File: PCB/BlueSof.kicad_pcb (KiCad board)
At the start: 2 copper layers, 137.2 x 109.2 mm, 66 parts, among them SW1 SW_PUSH, SW10 SW_PUSH, SW11 SW_PUSH, SW12 SW_PUSH, SW13 SW_PUSH, SW14 SW_PUSH, SW15 SW_PUSH, SW16 SW_PUSH, SW17 SW_PUSH, SW18 SW_PUSH, SW19 SW_PUSH, SW2 SW_PUSH, SW20 SW_PUSH, SW21 SW_PUSH, SW22 SW_PUSH, SW23 SW_PUSH, SW24 SW_PUSH, SW25 Rotary_Encoder_Switch, SW26 SW_PUSH, SW27 SW_PUSH, SW28 SW_PUSH, SW29 SW_PUSH, SW3 SW_PUSH, SW30 SW_PUSH, SW4 SW_PUSH, SW5 SW_PUSH, SW6 SW_PUSH, SW7 SW_PUSH, SW8 SW_PUSH, SW9 SW_PUSH

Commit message: initial layout
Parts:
- removed TH1, TH3, TH4, TH5, TH6, TH7: HOLE, MountingHole:MountingHole_4mm
- added C1: 4.7uF, Capacitor_SMD:C_0603_1608Metric_Pad1.08x0.95mm_HandSolder, F.Cu at (103.5, 62.0)
- added C2: 4.7uF, Capacitor_SMD:C_0603_1608Metric_Pad1.08x0.95mm_HandSolder, F.Cu at (110.5, 56.9)
- added C3: 22pF, Capacitor_SMD:C_0603_1608Metric_Pad1.08x0.95mm_HandSolder, F.Cu at (110.5, 110.3)
- added C4: 22pF, Capacitor_SMD:C_0603_1608Metric_Pad1.08x0.95mm_HandSolder, F.Cu at (112.4, 114.9)
- added C5: 10uF, Capacitor_SMD:C_0603_1608Metric_Pad1.08x0.95mm_HandSolder, F.Cu at (106.0, 49.9)
- added D31: LED, LED_SMD:LED_0603_1608Metric_Pad1.05x0.95mm_HandSolder, F.Cu at (104.0, 49.9)
- added D32: LED, LED_SMD:LED_0603_1608Metric_Pad1.05x0.95mm_HandSolder, F.Cu at (91.0, 49.9)
- added D33: 1N5819, Diode_SMD:D_SOD-323_HandSoldering, F.Cu at (104.2, 57.9)
- added J1: USB_C_Receptacle_USB2.0, Connector_USB:USB_C_Receptacle_HRO_TYPE-C-31-M-12, F.Cu at (97.5, 50.4)
- added J2: Conn_01x01_Female, Connector_PinHeader_2.54mm:PinHeader_1x01_P2.54mm_Vertical, F.Cu at (95.0, 61.9)
- added J3: Conn_01x04_Female, Connector_PinHeader_2.54mm:PinHeader_1x04_P2.54mm_Vertical, F.Cu at (130.5, 82.7)
- added J4: Conn_01x01_Female, Connector_PinHeader_2.54mm:PinHeader_1x01_P2.54mm_Vertical, F.Cu at (106.2, 61.9)
- added Q2: A03407, Package_TO_SOT_SMD:SOT-23, F.Cu at (109.0, 53.4)
- added R1: 10k, Resistor_SMD:R_0603_1608Metric_Pad0.98x0.95mm_HandSolder, F.Cu at (104.0, 53.5)
- added R2: 10k, Resistor_SMD:R_0603_1608Metric_Pad0.98x0.95mm_HandSolder, F.Cu at (97.8, 62.1)
- added R4: 820k, Resistor_SMD:R_0603_1608Metric_Pad0.98x0.95mm_HandSolder, F.Cu at (107.5, 56.9)
- added R5: 2M, Resistor_SMD:R_0603_1608Metric_Pad0.98x0.95mm_HandSolder, F.Cu at (109.0, 56.9)
- added R6: 10k, Resistor_SMD:R_0603_1608Metric_Pad0.98x0.95mm_HandSolder, F.Cu at (91.0, 53.5)
- added R7: 5.1k, Resistor_SMD:R_0603_1608Metric_Pad0.98x0.95mm_HandSolder, F.Cu at (97.0, 57.9)
- added R8: 5.1k, Resistor_SMD:R_0603_1608Metric_Pad0.98x0.95mm_HandSolder, F.Cu at (93.4, 57.9)
- added R9: 100k, Resistor_SMD:R_0603_1608Metric_Pad0.98x0.95mm_HandSolder, F.Cu at (100.5, 57.9)
- added SW31: SW_Push, Button_Switch_SMD:SW_SPST_B3U-1000P, F.Cu at (92.5, 120.4)
- added U1: LN2054Y42AMR, Package_TO_SOT_SMD:SOT-23-5, F.Cu at (100.5, 62.1)
- added U2: E73-2G4M08S1C, BlueSof:E73-2G4M08S1C-52840, F.Cu at (108.0, 109.9)
- added U3: AP2112K-3.3, Package_TO_SOT_SMD:SOT-23-5, F.Cu at (109.0, 49.9)
- added Y1: 32.768kHz, Crystal:Crystal_SMD_MicroCrystal_CM9V-T1A-2Pin_1.6x1.0mm_HandSoldering, F.Cu at (109.5, 114.0)
- D1, D10, D11, D12, D13, D14, D15, D16, D17, D18, D19, D2, D20, D21, D22, D23, D24, D25, D26, D27, D28, D29, D3, D30, D4, D5, D6, D7, D8, D9: footprint SofleKeyboard-footprint:Diode_SOD123 -> BlueSof:Diode_SOD123
- SW1, SW10, SW11, SW12, SW13, SW14, SW15, SW16, SW17, SW18, SW19, SW2, SW20, SW21, SW22, SW23, SW24, SW27, SW28, SW29, SW3, SW30, SW4, SW5, SW6, SW7, SW8, SW9: footprint SofleKeyboard-footprint:KailhLowProfile -> BlueSof:KailhLowProfile
- SW26: footprint SofleKeyboard-footprint:KailhLowProfile -> BlueSof:KailhLowProfile_1.5U
- moved D25 21.1 mm to (111.0, 91.7), turned to 270 degrees
- moved SW25 9.51 mm to (93.0, 92.4)
- moved D26 5.41 mm to (112.5, 123.7)
- moved SW26 5.34 mm to (108.5, 126.2)
- moved SW27 1.00 mm to (130.0, 122.4), turned to 5 degrees
- moved SW30 0.80 mm to (185.0, 124.7)
- moved D27 0.26 mm to (129.7, 117.7), turned to 185 degrees
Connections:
- net SW25B renamed Net-(D25-Pad2)
- SW25 pad A: (no net) -> ENCA
- SW25 pad B: (no net) -> ENCB
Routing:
- removed copper zone on B.Cu, net GND
- removed copper zone on F.Cu, net GND
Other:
- board size 137.2 x 109.2 mm -> 132.5 x 106 mm
- board text added: "BlueSof v1 by ERL"
- board text removed: "Ellow Sofle Keyboard v1 by ERL"

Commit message: before 2nd side
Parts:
- moved + 15.0 mm to (110.0, 61.7)
- moved - 12.8 mm to (93.5, 61.7)
- moved Y1 0.27 mm to (109.5, 113.7)
- renumbered J2 to +, J4 to -
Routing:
- net VBUS: track 0.00 -> 91.9 mm
- net VDD_H: track 0.00 -> 72.0 mm
- net VBAT: track 0.00 -> 29.2 mm
- net Net-(C3-Pad2): track 0.00 -> 4.14 mm
- net Net-(C4-Pad2): track 0.00 -> 4.10 mm
- added copper zone on F.Cu, net (none)
- added copper zone on B.Cu, net GND

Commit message: EOD, layout on side 2 done, not routed
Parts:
- added C10: 10uF, Capacitor_SMD:C_0603_1608Metric_Pad1.08x0.95mm_HandSolder, B.Cu at (106.0, 49.9)
- added C6: 22pF, Capacitor_SMD:C_0603_1608Metric_Pad1.08x0.95mm_HandSolder, B.Cu at (111.1, 108.0)
- added C7: 22pF, Capacitor_SMD:C_0603_1608Metric_Pad1.08x0.95mm_HandSolder, B.Cu at (111.1, 104.4)
- added C8: 4.7uF, Capacitor_SMD:C_0603_1608Metric_Pad1.08x0.95mm_HandSolder, B.Cu at (103.5, 61.1)
- added C9: 4.7uF, Capacitor_SMD:C_0603_1608Metric_Pad1.08x0.95mm_HandSolder, B.Cu at (110.5, 56.9)
- added D34: LED, LED_SMD:LED_0603_1608Metric_Pad1.05x0.95mm_HandSolder, B.Cu at (91.7, 49.9)
- added D35: 1N5819, Diode_SMD:D_SOD-323_HandSoldering, B.Cu at (104.2, 57.1)
- added D36: LED, LED_SMD:LED_0603_1608Metric_Pad1.05x0.95mm_HandSolder, B.Cu at (90.2, 49.9)
- added J5: USB_C_Receptacle_USB2.0, Connector_USB:USB_C_Receptacle_HRO_TYPE-C-31-M-12, B.Cu at (97.8, 50.4)
- added Q1: A03407, Package_TO_SOT_SMD:SOT-23, B.Cu at (109.0, 53.4)
- added R10: 2M, Resistor_SMD:R_0603_1608Metric_Pad0.98x0.95mm_HandSolder, B.Cu at (109.0, 56.9)
- added R11: 10k, Resistor_SMD:R_0603_1608Metric_Pad0.98x0.95mm_HandSolder, B.Cu at (91.7, 53.5)
- added R12: 5.1k, Resistor_SMD:R_0603_1608Metric_Pad0.98x0.95mm_HandSolder, B.Cu at (97.0, 57.9)
- added R13: 5.1k, Resistor_SMD:R_0603_1608Metric_Pad0.98x0.95mm_HandSolder, B.Cu at (93.5, 57.9)
- added R14: 100k, Resistor_SMD:R_0603_1608Metric_Pad0.98x0.95mm_HandSolder, B.Cu at (100.5, 57.9)
- added R15: 10k, Resistor_SMD:R_0603_1608Metric_Pad0.98x0.95mm_HandSolder, B.Cu at (90.2, 53.5)
- added R16: 10k, Resistor_SMD:R_0603_1608Metric_Pad0.98x0.95mm_HandSolder, B.Cu at (97.8, 61.4)
- added R3: 820k, Resistor_SMD:R_0603_1608Metric_Pad0.98x0.95mm_HandSolder, B.Cu at (107.5, 56.9)
- added SW32: SW_Push, Button_Switch_SMD:SW_SPST_B3U-1000P, B.Cu at (92.5, 120.4)
- added U4: E73-2G4M08S1C, BlueSof:E73-2G4M08S1C-52840_NoInsidePads, B.Cu at (108.0, 109.9)
- added U5: LN2054Y42AMR, Package_TO_SOT_SMD:SOT-23-5, B.Cu at (100.5, 61.4)
- added U6: AP2112K-3.3, Package_TO_SOT_SMD:SOT-23-5, B.Cu at (109.0, 49.9)
- added Y2: 32.768kHz, Crystal:Crystal_SMD_MicroCrystal_CM9V-T1A-2Pin_1.6x1.0mm_HandSoldering, B.Cu at (109.4, 106.1)
- U2: footprint BlueSof:E73-2G4M08S1C-52840 -> BlueSof:E73-2G4M08S1C-52840_NoInsidePads
- moved D31 13.8 mm to (90.2, 49.9)
- moved R1 13.8 mm to (90.2, 53.5)
- moved C1 0.75 mm to (103.5, 61.3)
- moved R2 0.75 mm to (97.8, 61.4)
- moved U1 0.75 mm to (100.5, 61.4)
- moved D32 0.70 mm to (91.7, 49.9)
- moved R6 0.70 mm to (91.7, 53.5)
- moved J1 0.35 mm to (97.8, 50.4)
- renumbered + to J2, - to J4
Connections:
- J3 pad 3: (no net) -> SWD
- R2 pad 1: PROG -> Net-(R2-Pad1)
- U1 pad 5: PROG -> Net-(R2-Pad1)
- U2 pad 10: PROG -> ENCA
- U2 pad 15: ENCA -> P0.05_2
- U2 pad 17: ENCB -> row0
- U2 pad 26: (no net) -> RESET
- U2 pad 33: row0 -> row1
- U2 pad 35: row1 -> row2
- U2 pad 37: row2 -> SWD
- U2 pad 9: RESET -> ENCB
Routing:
- net VBUS: track 91.9 -> 0.00 mm
- net VDD_H: track 72.0 -> 0.00 mm
- net VBAT: track 29.2 -> 0.00 mm
- net Net-(C3-Pad2): track 4.14 -> 0.00 mm
- net Net-(C4-Pad2): track 4.10 -> 0.00 mm
- added copper zone on F.Cu, net Net-(U4-Pad42)
- removed copper zone on F.Cu, net (none)
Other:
- net class GND: clearance 0.2 -> 0.25; trace_width 0.5 -> 0.3
- net class VCC: clearance 0.2 -> 0.25; trace_width 0.5 -> 0.3

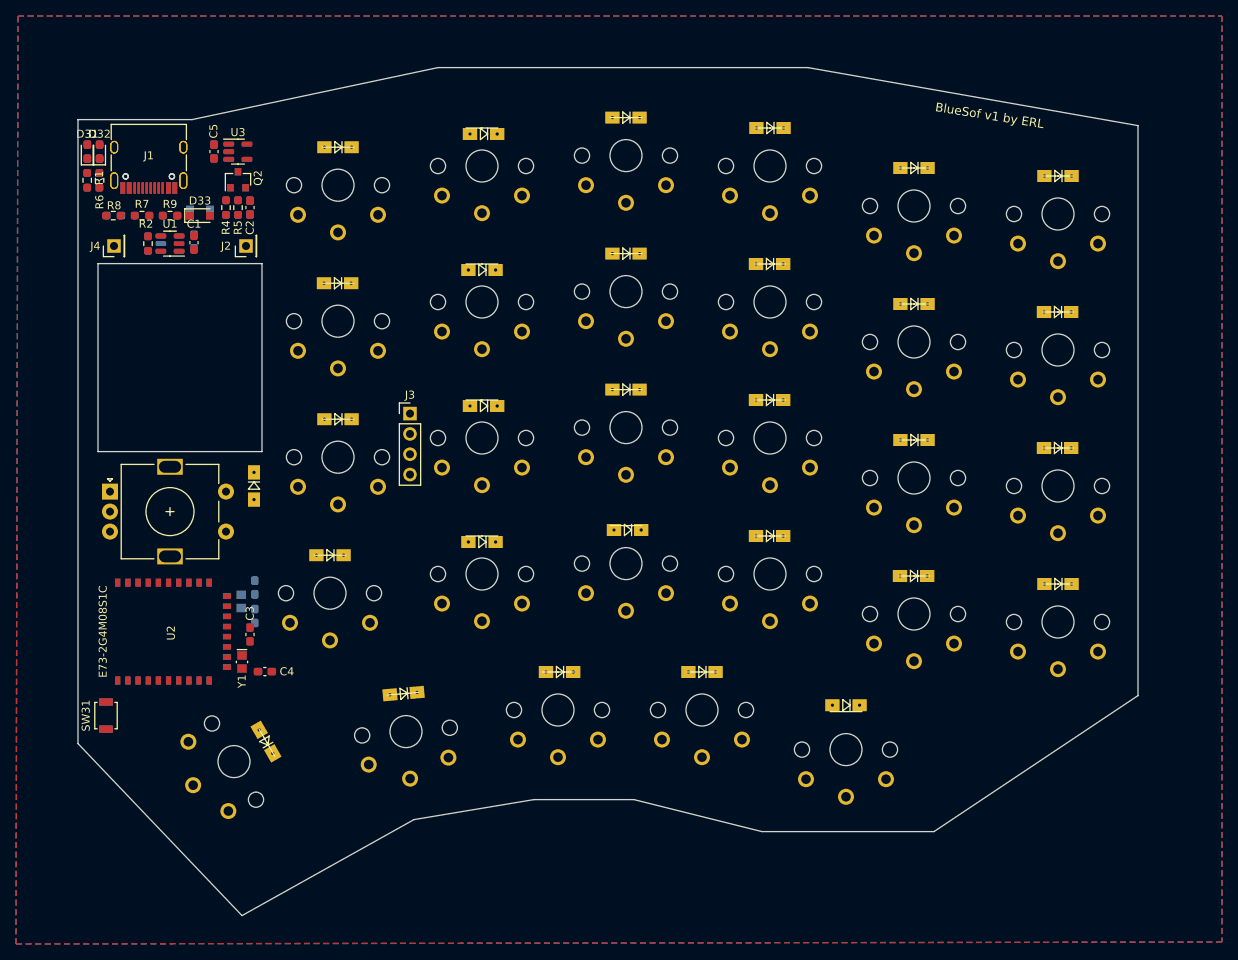
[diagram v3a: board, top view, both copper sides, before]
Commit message: autoroute done, still needs cleanup
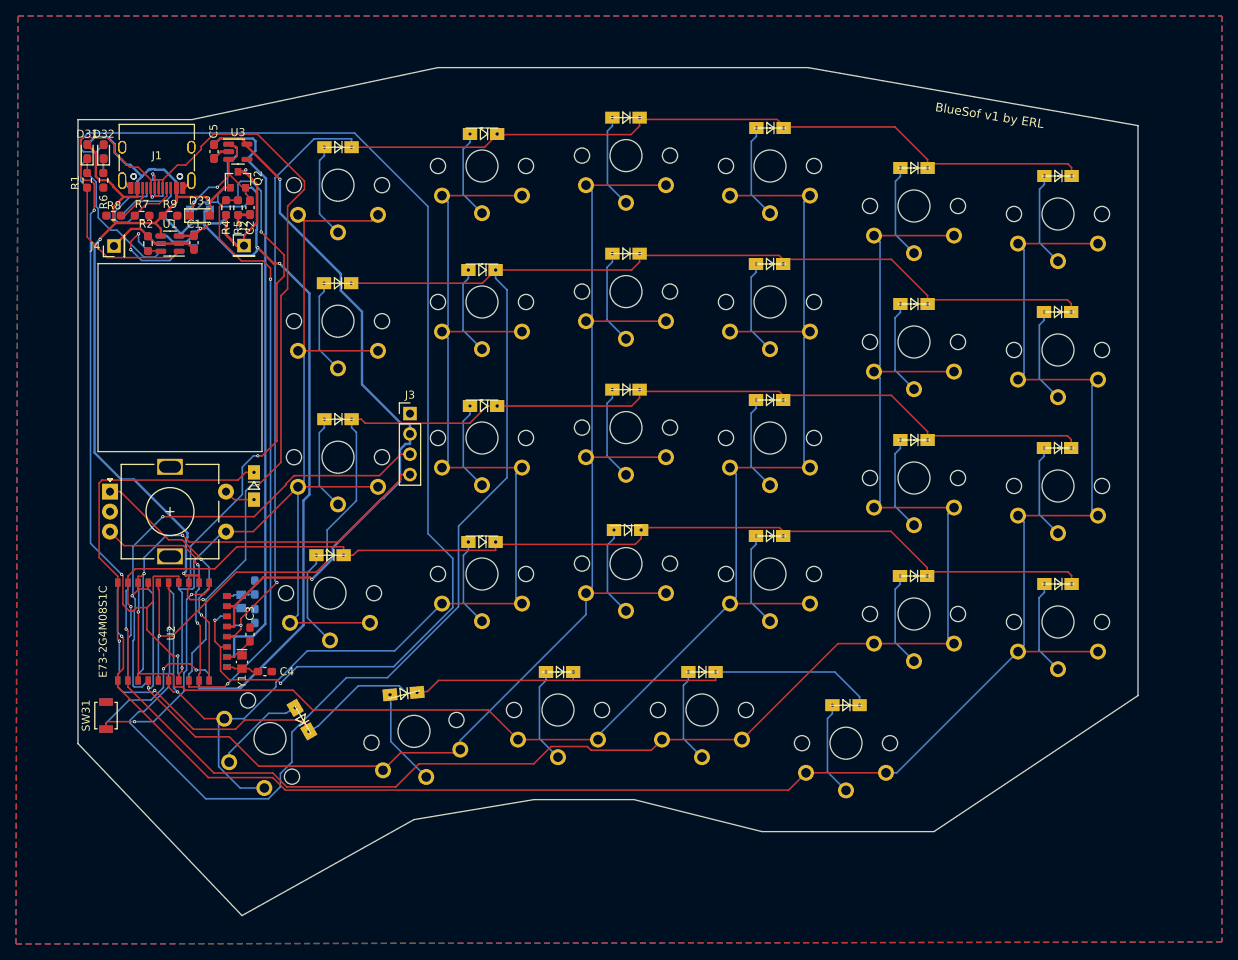
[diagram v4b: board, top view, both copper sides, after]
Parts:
- moved SW26 5.34 mm to (113.0, 123.3)
- moved D26 5.27 mm to (117.0, 120.9)
- moved SW27 1.00 mm to (131.0, 122.4), turned to 15 degrees
- moved J1 1.00 mm to (98.8, 50.4)
- moved J5 1.00 mm to (98.8, 50.4)
- moved SW30 0.80 mm to (185.0, 123.8)
- moved D32 0.50 mm to (92.2, 49.9)
- moved D34 0.50 mm to (92.2, 49.9)
- moved R11 0.50 mm to (92.2, 53.5)
- moved R6 0.50 mm to (92.2, 53.5)
- moved J2 0.25 mm to (109.8, 61.6), turned to 0 degrees
- turned R1 to 270 degrees
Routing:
- net col0: track 0.00 -> 231.5 mm, vias 0 -> 1
- net row1: track 0.00 -> 220.4 mm, vias 0 -> 1
- net col1: track 0.00 -> 212.3 mm, vias 0 -> 1
- net col2: track 0.00 -> 190.6 mm, vias 0 -> 1
- net col3: track 0.00 -> 178.2 mm, vias 0 -> 1
- net row0: track 0.00 -> 171.8 mm, vias 0 -> 2
- net col4: track 0.00 -> 163.0 mm, vias 0 -> 1
- net row2: track 0.00 -> 154.2 mm, vias 0 -> 2
- net row4: track 0.00 -> 150.6 mm, vias 0 -> 2
- net P0.05_2: track 0.00 -> 146.2 mm, vias 0 -> 2
- net row3: track 0.00 -> 141.8 mm, vias 0 -> 1
- net col5: track 0.00 -> 126.7 mm, vias 0 -> 1
- net VBUS2: track 0.00 -> 116.8 mm, vias 0 -> 2
- net DATA-: track 0.00 -> 103.6 mm, vias 0 -> 3
- net DATA+: track 0.00 -> 103.1 mm, vias 0 -> 4
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- added copper zone on F.Cu, net GND
- removed copper zone on F.Cu, net Net-(U4-Pad42)

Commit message: making progress on autoroute cleanup
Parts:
- added REF**: MountingHole_2.7mm_M2.5, MountingHole:MountingHole_2.7mm_M2.5, F.Cu at (96.3, 124.6)
- added REF**: MountingHole_2.7mm_M2.5, MountingHole:MountingHole_2.7mm_M2.5, F.Cu at (130.5, 111.1)
- added REF**: MountingHole_2.7mm_M2.5, MountingHole:MountingHole_2.7mm_M2.5, F.Cu at (202.5, 99.1)
- added REF**: MountingHole_2.7mm_M2.5, MountingHole:MountingHole_2.7mm_M2.5, F.Cu at (202.5, 66.1)
- added REF**: MountingHole_2.7mm_M2.5, MountingHole:MountingHole_2.7mm_M2.5, F.Cu at (130.5, 62.6)
- moved D26 4.54 mm to (113.0, 123.1)
- moved SW26 4.53 mm to (109.0, 125.4)
- moved C4 4.06 mm to (108.5, 113.7), turned to 270 degrees
- moved C7 3.92 mm to (107.2, 103.7), turned to 180 degrees
- moved C6 3.33 mm to (108.3, 106.2), turned to 270 degrees
- moved C3 3.13 mm to (107.5, 111.2), turned to 180 degrees
- moved Y2 2.80 mm to (106.6, 106.2)
- moved D31 2.80 mm to (87.3, 49.9)
- moved R1 2.80 mm to (87.3, 53.5)
- moved R15 2.80 mm to (87.3, 53.5)
- moved D25 2.80 mm to (108.2, 91.7)
- moved D33 2.80 mm to (101.5, 57.9)
- moved D35 2.80 mm to (101.5, 57.1)
- moved D36 2.80 mm to (87.4, 49.9)
- moved J2 2.80 mm to (107.0, 61.6)
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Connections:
- D32 pad 2: (no net) -> P0.05
- U2 pad 15: P0.05_2 -> P0.05
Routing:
- net P0.05: track 0.00 -> 77.3 mm, vias 0 -> 2
- net P0.05_2: track 146.2 -> 87.7 mm, vias 2 -> 0
- net row1: track 220.4 -> 164.6 mm, vias 1 -> 2
- net VBUS: track 91.3 -> 129.3 mm
- net GND: track 28.0 -> 47.5 mm, vias 1 -> 7
- net RESET: track 27.9 -> 43.0 mm
- net VDD_H: track 89.4 -> 100.8 mm, vias 2 -> 0
- net col5: track 126.7 -> 137.4 mm
- net row3: track 141.8 -> 149.6 mm
- net DATA-: track 103.6 -> 96.1 mm, vias 3 -> 4
- net Net-(R16-Pad1): track 12.1 -> 4.93 mm, vias 2 -> 0
- net BATTERY_MEASURE2: track 62.8 -> 56.4 mm
- net RESET2: track 19.4 -> 13.1 mm, vias 2 -> 0
- net Net-(J1-PadB5): track 4.91 -> 10.9 mm
- net row4: track 150.6 -> 155.6 mm, vias 2 -> 1
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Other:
- board size 132.5 x 106 mm -> 135.3 x 106 mm

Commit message: EOD
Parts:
- moved D30 2.19 mm to (187.0, 120.0)
- moved SW30 2.08 mm to (186.9, 124.7)
- moved D28 2.00 mm to (151.2, 115.0)
- moved D29 2.00 mm to (169.0, 115.0)
- moved SW28 2.00 mm to (151.0, 119.7)
- moved SW29 2.00 mm to (169.0, 119.7)
- moved D27 0.31 mm to (130.0, 117.7), turned to 195 degrees
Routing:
- net GND: track 47.5 -> 54.7 mm, vias 7 -> 24
- net VDD_H2: track 76.6 -> 78.6 mm
- net row4: track 155.6 -> 157.1 mm
- net col2: track 193.7 -> 195.2 mm
- net col0: track 233.9 -> 235.2 mm
- net row3: track 149.6 -> 150.4 mm
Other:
- board size 135.3 x 106 mm -> 135.3 x 104.9 mm
- board text added: "CUTOUT"

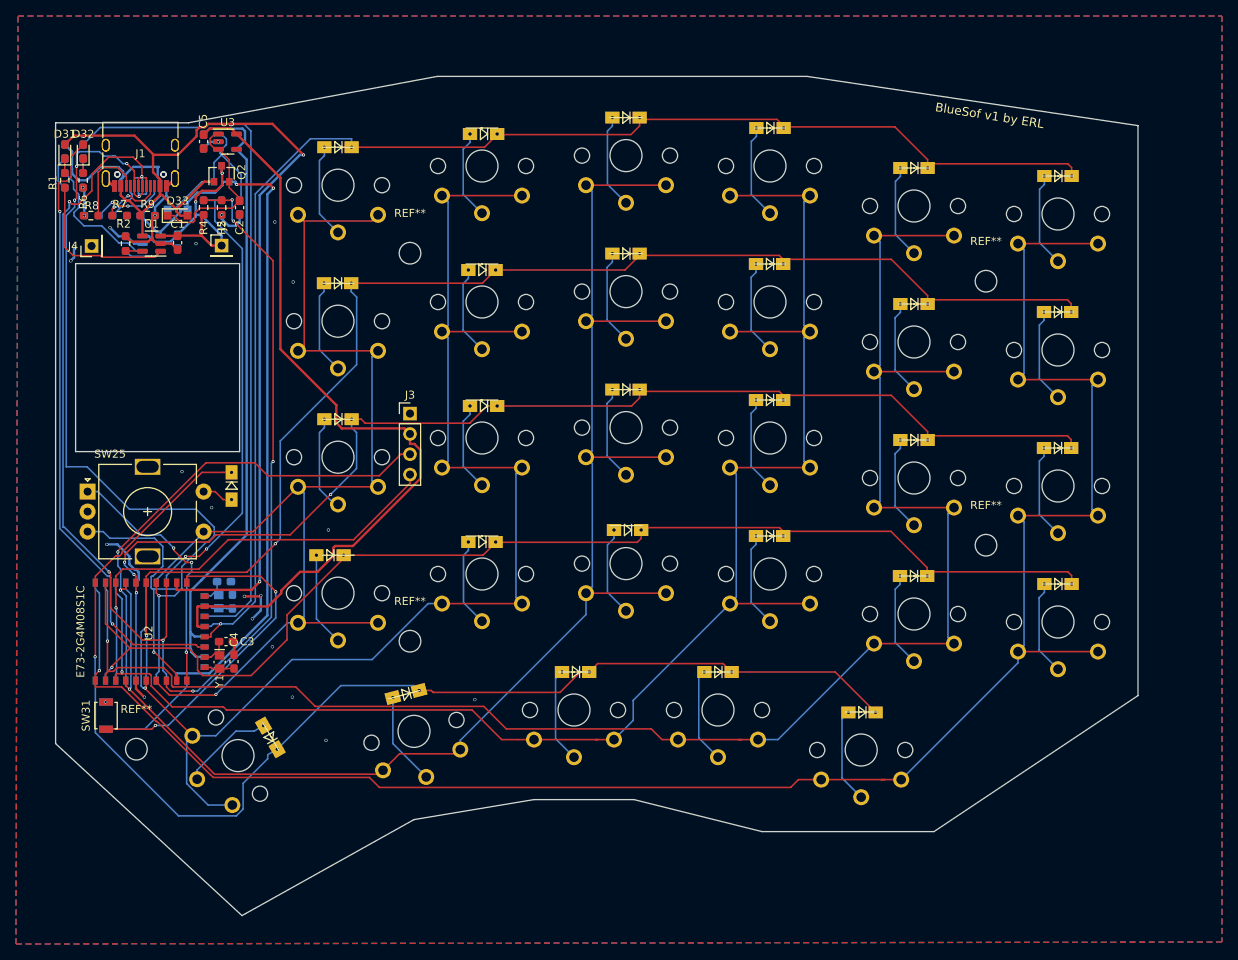
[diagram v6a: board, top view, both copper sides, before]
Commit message: ordered first boards
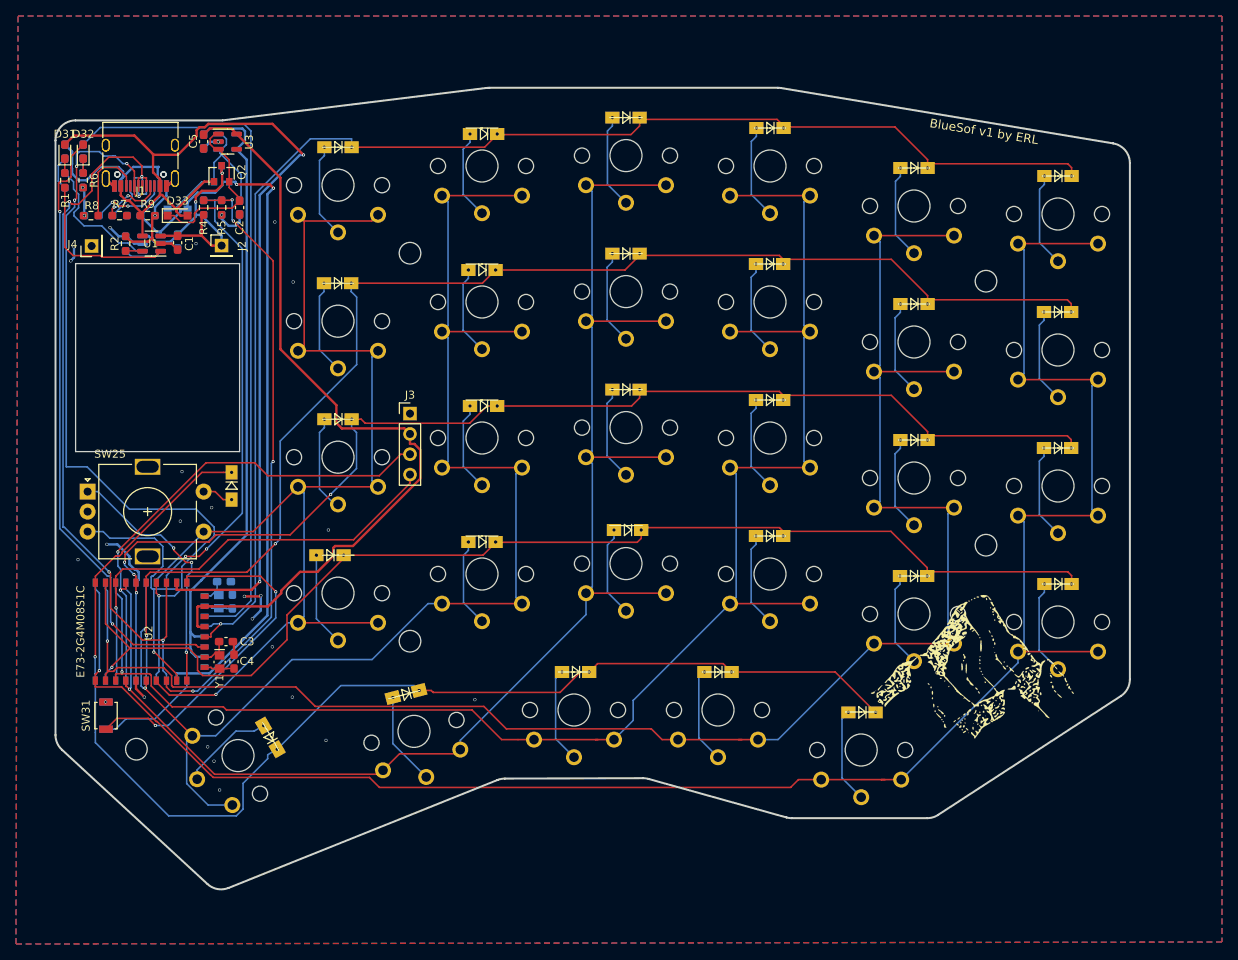
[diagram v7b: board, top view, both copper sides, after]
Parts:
- added ?: , , F.Cu at (206.5, 119.3)
- added G***: LOGO, BlueSof:mountain, F.Cu at (200.8, 114.3)
- added G***: LOGO, BlueSof:mountain, B.Cu at (202.3, 114.1)
- R1, R11, R15, R6: value 10k -> 1k
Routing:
- net RESET: track 43.0 -> 43.7 mm
- net row4: track 157.1 -> 157.8 mm
- net GND: vias 24 -> 29
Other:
- board size 135.3 x 104.9 mm -> 134.3 x 100.2 mm
